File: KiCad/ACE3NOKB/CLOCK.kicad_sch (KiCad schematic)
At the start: 10 parts, among them J302 Conn_01x03, J303 Conn_01x03, SW301 EG2305, X301 6.5536 MHz

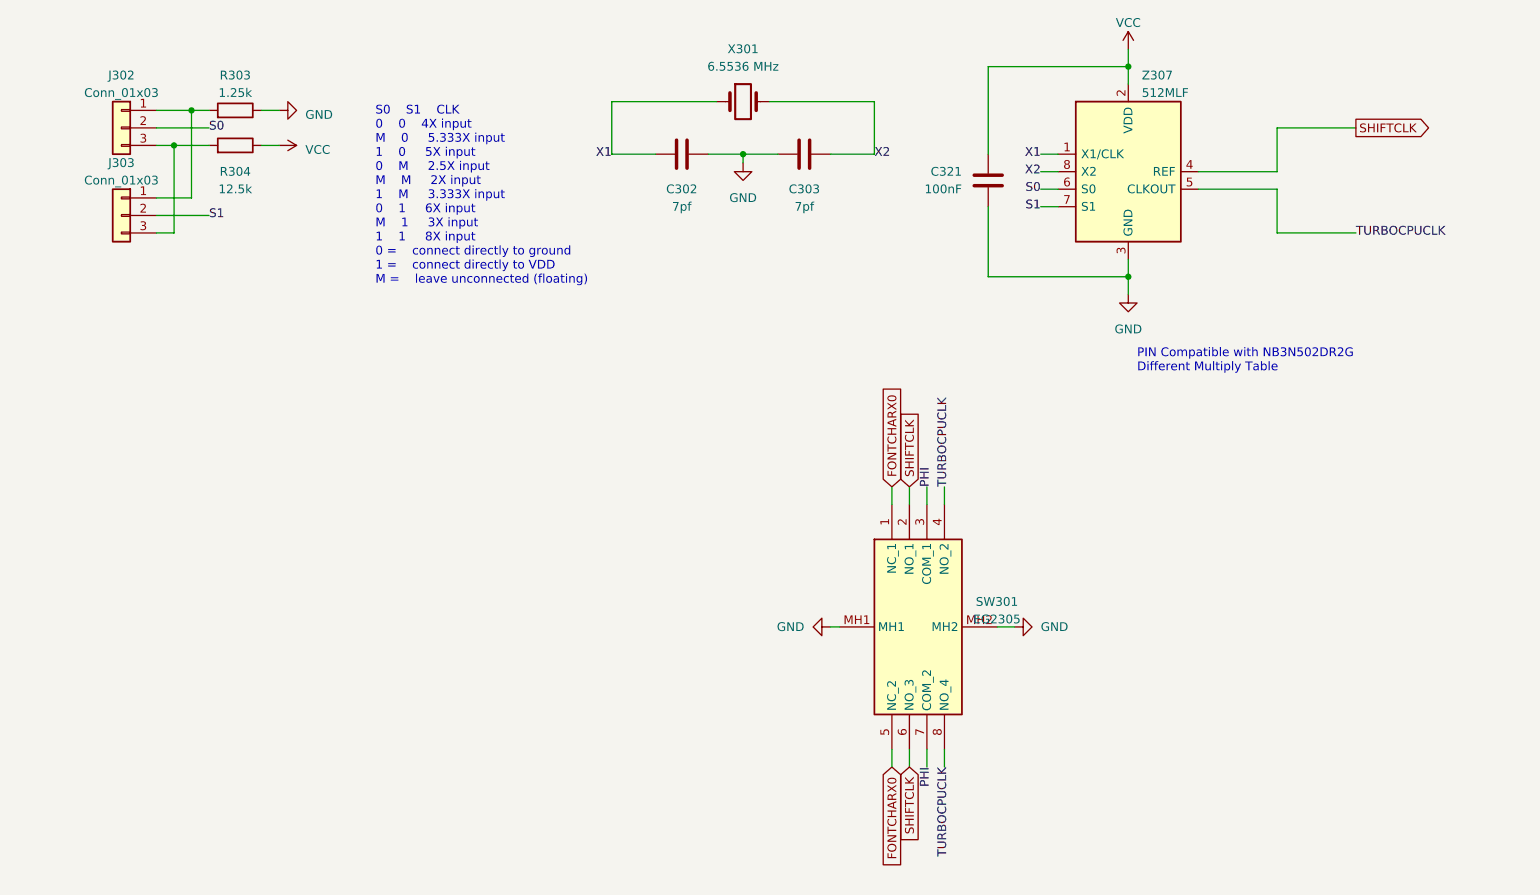
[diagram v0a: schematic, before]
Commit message: Update, with new Clock Multiplier and Wait functionality.
Signed-off-by: John Bradley <flypie@rocketmail.com>
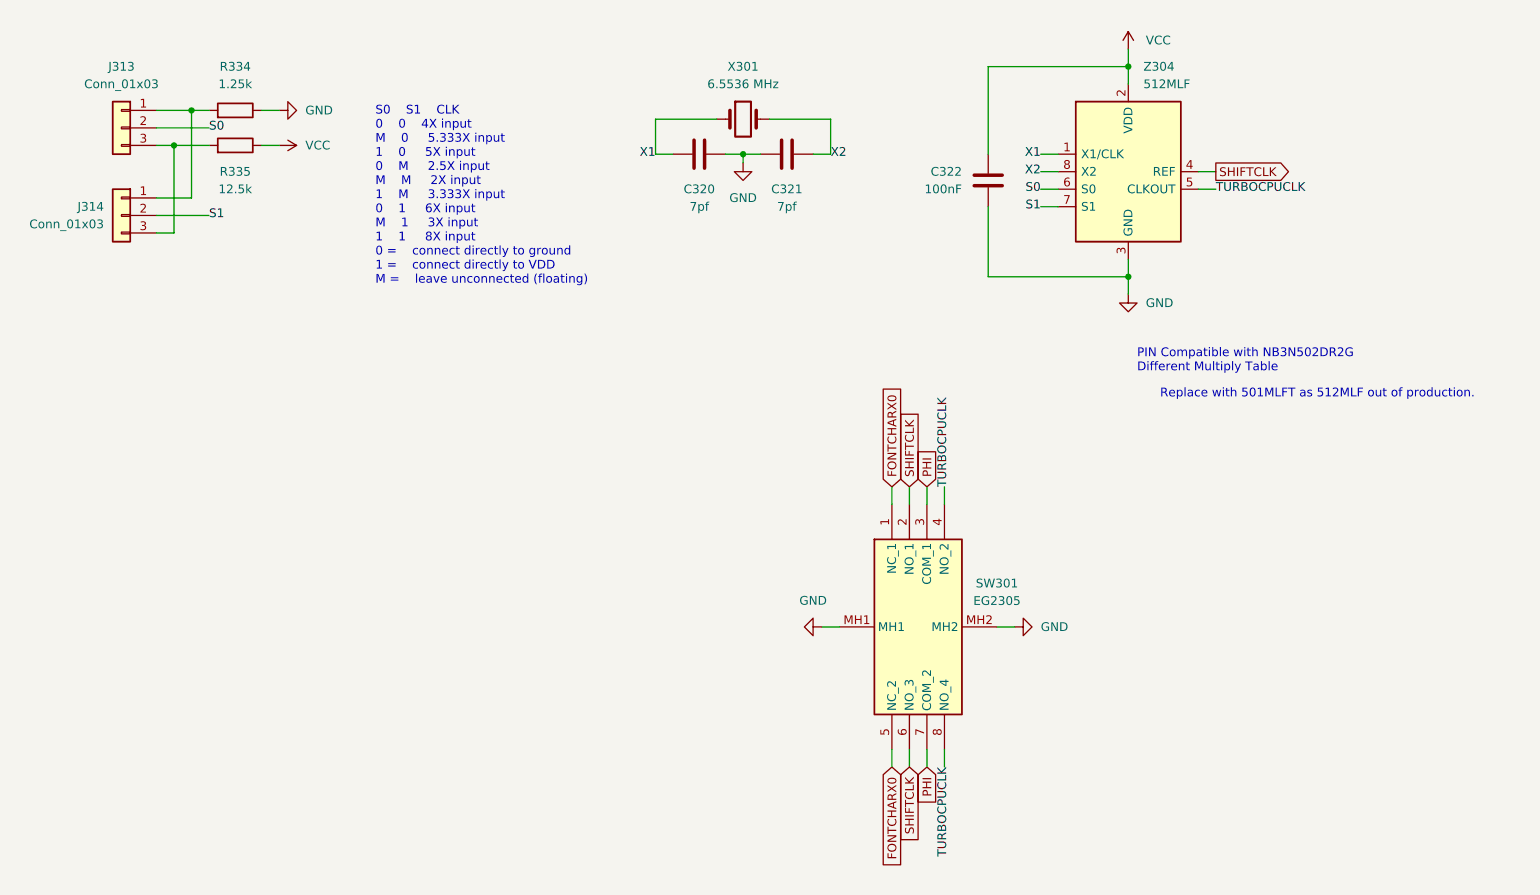
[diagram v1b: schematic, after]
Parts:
- C322: renamed from C321; footprint Capacitor_THT:C_Rect_L7.0mm_W2.0mm_P5.00mm -> Capacitor_THT:C_Disc_D4.3mm_W1.9mm_P5.00mm
- R334: renamed from R303; footprint Resistor_THT:R_Axial_DIN0204_L3.6mm_D1.6mm_P1.90mm_Vertical -> Resistor_THT:R_Axial_DIN0204_L3.6mm_D1.6mm_P2.54mm_Vertical
- R335: renamed from R304; footprint Resistor_THT:R_Axial_DIN0204_L3.6mm_D1.6mm_P1.90mm_Vertical -> Resistor_THT:R_Axial_DIN0204_L3.6mm_D1.6mm_P2.54mm_Vertical
- renumbered C302 to C320, C303 to C321, J302 to J313, J303 to J314, Z307 to Z304
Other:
- note added: "Replace with 501MLFT as 512MLF out of production."
- moved on the sheet: C320, C321, X301

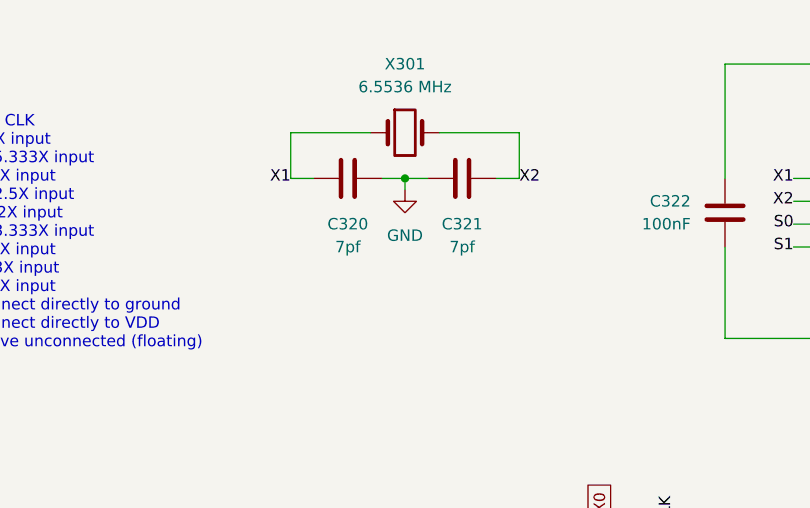
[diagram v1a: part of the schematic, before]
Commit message: Change Address decode to speed up the use of /WAIT to avoid conflicts when setting up character RAM. Rerange priority on Internal external /WAIT. Reconnect Clock to rest of circuit.
Signed-off-by: John Bradley <flypie@rocketmail.com>
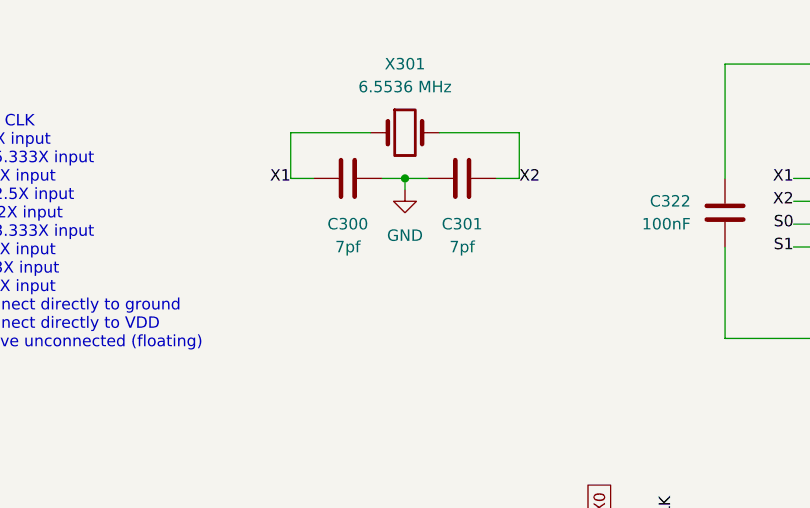
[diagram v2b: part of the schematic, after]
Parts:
- renumbered C320 to C300, C321 to C301
